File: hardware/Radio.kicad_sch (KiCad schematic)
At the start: 44 parts, among them Q305 BCX56, U801 RF69, U802 AS193-73LF, Y801 32_Mhz

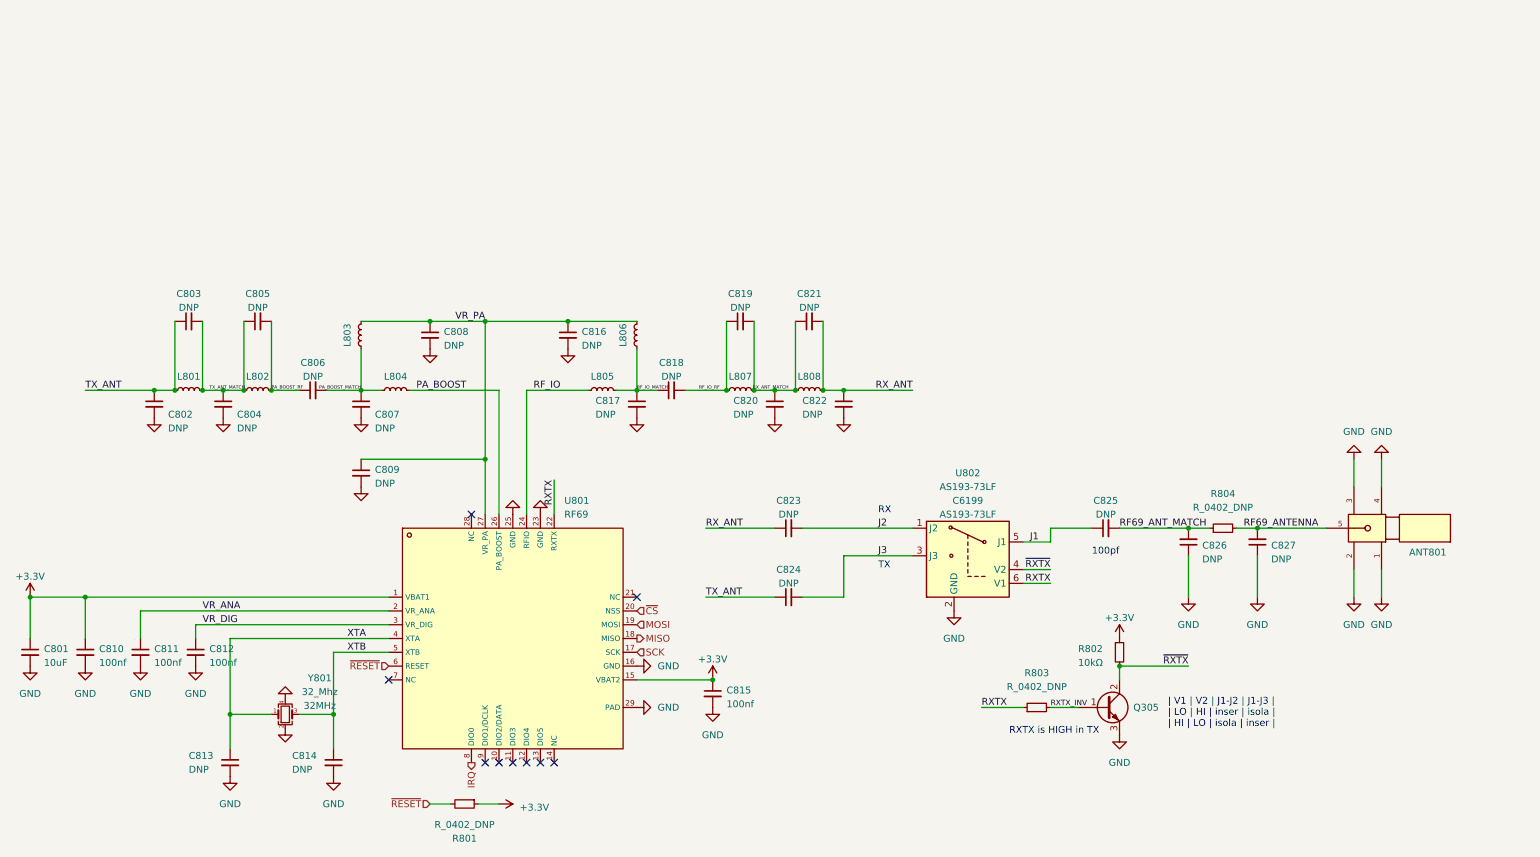
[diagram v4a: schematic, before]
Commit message: RF layout updates
Signed-off-by: Connor Rigby <connorr@hey.com>
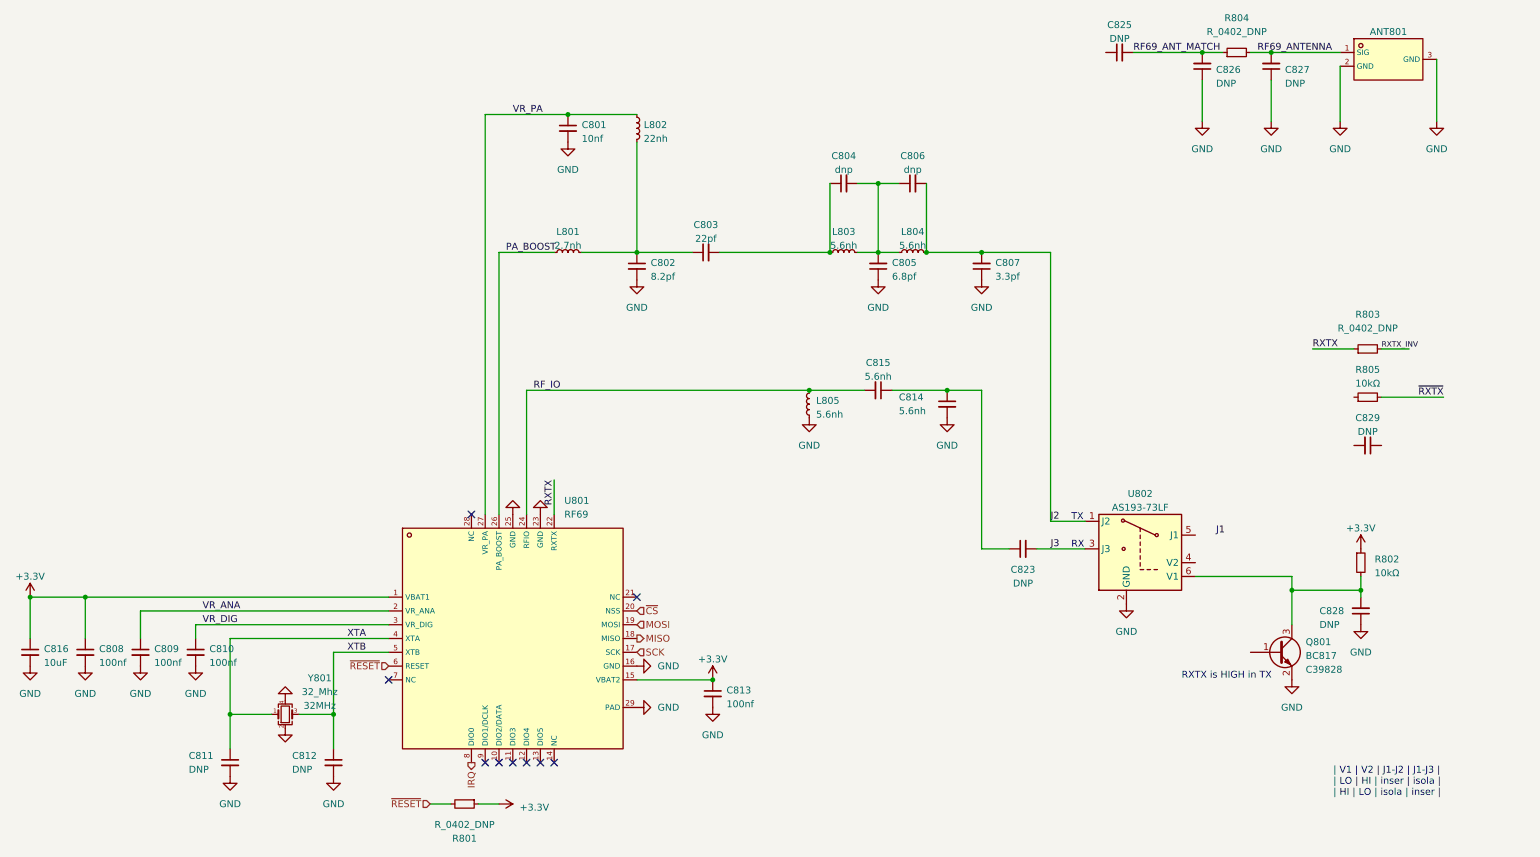
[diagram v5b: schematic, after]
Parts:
- removed ANT801: BWSMA-KE-P001, LCSC_Antenna:SMA-SMD_BWSMA-KE-P001, symbol LCSC_Antenna:BWSMA-KE-P001
- removed C801: C_0805_10u_X5R, Capacitor_SMD:C_0805_2012Metric, symbol LCSC_Capacitor:C_0805_10u_X5R
- removed C808, C809, C816, C817, C818, C819, C820, C821, C822, C824: C_0402_DNP, Capacitor_SMD:C_0402_1005Metric, symbol LCSC_Capacitor:C_0402_DNP
- removed L801, L802, L803, L804, L805, L806, L807, L808: L_0402_DNP, Inductor_SMD:L_0402_1005Metric, symbol LCSC_Inductor:L_0402_DNP
- removed Q305: BCX56, Package_TO_SOT_SMD:SOT-89-3, symbol LCSC_Transistor:BCX56
- added ANT801: BWIPX-1-001E, LCSC_Antenna:IPEX-SMD_BWIPX-1-001E, symbol LCSC_Antenna:BWIPX-1-001E
- added C801, C814, C815, C828, C829: C_0402_DNP, Capacitor_SMD:C_0402_1005Metric, symbol LCSC_Capacitor:C_0402_DNP
- added C816: C_0805_10u_X5R, Capacitor_SMD:C_0805_2012Metric, symbol LCSC_Capacitor:C_0805_10u_X5R
- added L801: 2.7nh, Inductor_SMD:L_0402_1005Metric, symbol Device:L_Small
- added L802: 22nh, Inductor_SMD:L_0402_1005Metric, symbol Device:L_Small
- added L803, L804, L805: 5.6nh, Inductor_SMD:L_0402_1005Metric, symbol Device:L_Small
- added Q801: BC817, Package_TO_SOT_SMD:SOT-23, symbol LCSC_Transistor1:BC817
- added R805: R_0402_10k, Resistor_SMD:R_0402_1005Metric, symbol LCSC_Resistor:R_0402_10k
- C802: Capacitance DNP -> 8.2pf
- C803: Capacitance DNP -> 22pf
- C804, C806: Capacitance DNP -> dnp
- C805: Capacitance DNP -> 6.8pf
- C807: Capacitance DNP -> 3.3pf
- renumbered C810 to C808, C811 to C809, C812 to C810, C813 to C811, C814 to C812, C815 to C813
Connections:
- net +3.3V: now also C816.1
- net GND: now also C805.1, C807.1, ANT801.2 (GND), ANT801.3 (GND), C801.2, C814.2, C816.2, C828.1, L805.1, Q801.2 (E); no longer C804.2, C807.2
- net J1: no longer C825.1, U802.5 (J1)
- net J2: now also C806.2, C807.2, L804.2; no longer C823.2
- net J3: now also C823.2
- net PA_BOOST: now also L801.1
- net RF69_ANTENNA: now also ANT801.1 (SIG)
- net RF_IO: now also C815.2, L805.2
- net RXTX: no longer U802.6 (V1)
- net VR_PA: now also C801.1, L802.1
- net ~{RXTX}: now also R805.2; no longer R802.2, U802.4 (V2)
- removed net PA_BOOST_MATCH: C806.2, C807.1
- net PA_BOOST_RF: no longer names the net of C805.2, C806.1
- net PA_BOOST_RF: now also C804.2, L803.2, L804.1
- net RX_ANT: no longer names the net of C823.1
- net RX_ANT: now also C814.1, C815.1
- net TX_ANT: no longer names the net of C802.1, C803.1
- net TX_ANT: now also L801.2, L802.2
- net TX_ANT_MATCH: no longer names the net of C803.2, C804.1
- net TX_ANT_MATCH: now also L803.1; no longer C805.1
- new net: C828.2, Q801.3 (C), R802.2, U802.6 (V1)
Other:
- note removed: "100pf"
- moved on the sheet: C823, C825, C826, C827, R802, R803, R804, U802

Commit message: Almost ready for fab
Signed-off-by: Connor Rigby <connorr@hey.com>
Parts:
- removed C801, C802, C803, C805, C807, C811, C812, C814, C815, C823, C825, C828, C829: C_0402_DNP, Capacitor_SMD:C_0402_1005Metric, symbol LCSC_Capacitor:C_0402_DNP
- removed L801: 2.7nh, Inductor_SMD:L_0402_1005Metric, symbol Device:L_Small
- removed L802: 22nh, Inductor_SMD:L_0402_1005Metric, symbol Device:L_Small
- removed L803, L804, L805: 5.6nh, Inductor_SMD:L_0402_1005Metric, symbol Device:L_Small
- removed R801, R803, R804: R_0402_DNP, Resistor_SMD:R_0402_1005Metric, symbol LCSC_Resistor:R_0402_DNP
- removed R802: R_0402_10k, Resistor_SMD:R_0402_1005Metric, symbol LCSC_Resistor:R_0402_10k
- added C801: C_0402_10n_C0G, Capacitor_SMD:C_0402_1005Metric, symbol LCSC_Capacitor:C_0402_10n_C0G
- added C802: C_0402_8p2_C0G, Capacitor_SMD:C_0402_1005Metric, symbol LCSC_Capacitor:C_0402_8p2_C0G
- added C803: C_0402_22p_C0G, Capacitor_SMD:C_0402_1005Metric, symbol LCSC_Capacitor:C_0402_22p_C0G
- added C805: C_0402_6p8_C0G, Capacitor_SMD:C_0402_1005Metric, symbol LCSC_Capacitor:C_0402_6p8_C0G
- added C807: C_0402_3p3_C0G, Capacitor_SMD:C_0402_1005Metric, symbol LCSC_Capacitor:C_0402_3p3_C0G
- added C811, C812: C_0402_33p_C0G, Capacitor_SMD:C_0402_1005Metric, symbol LCSC_Capacitor:C_0402_33p_C0G
- added C814: C_0402_5p6_C0G, Capacitor_SMD:C_0402_1005Metric, symbol LCSC_Capacitor:C_0402_5p6_C0G
- added C815, L803, L804: L_0402_5n6, Inductor_SMD:L_0402_1005Metric, symbol LCSC_Inductor:L_0402_5n6
- added C823, C825: C_0402_100p_C0G, Capacitor_SMD:C_0402_1005Metric, symbol LCSC_Capacitor:C_0402_100p_C0G
- added C828, C829: C_0402_1nf_X7R, Capacitor_SMD:C_0402_1005Metric, symbol LCSC_Capacitor:C_0402_1nf_X7R
- added L801: L_0402_2n7, Inductor_SMD:L_0402_1005Metric, symbol LCSC_Inductor:L_0402_2n7
- added L802: L_0402_22n, Inductor_SMD:L_0402_1005Metric, symbol LCSC_Inductor:L_0402_22n
- added L805: L_0402_120n, Inductor_SMD:L_0402_1005Metric, symbol LCSC_Inductor:L_0402_120n
- added R801, R802, R803: R_0402_100k, Resistor_SMD:R_0402_1005Metric, symbol LCSC_Resistor:R_0402_100k
- added R804: R_0402_0, Resistor_SMD:R_0402_1005Metric, symbol LCSC_Resistor:R_0402_0
- C804, C806: Capacitance dnp -> DNP; now not fitted
- C826, C827: now not fitted
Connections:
- net ~{RXTX} is gone; now on net RXTX_NOR: R805.2
- net +3.3V: now also R801.1, R802.1
- net GND: now also C801.2, C802.2, C805.1, C807.1, C811.2, C812.2, C814.2, C828.1, C829.1, L805.1
- net J1: now also U802.5 (J1), C825.1
- net J2: now also C807.2, L804.2
- net J3: now also C823.2
- net PA_BOOST: now also L801.1
- net RF69_ANTENNA: now also R804.2
- net RF69_ANT_MATCH: now also C825.2, R804.1
- net RF_IO: now also C815.2, L805.2
- net RXTX: now also R805.1, R803.1
- net VR_PA: now also C801.1, L802.1
- net XTA: now also C811.1
- net XTB: now also C812.1
- net ~{RESET}: now also R801.2
- net V2: now reaches U802.4 (V2)
- net V2: now also C829.2, R803.2
- net V1: now reaches Q801.3 (C), U802.6 (V1)
- net V1: now also C828.2, R802.2
- net RXTX_NOR: now reaches Q801.1 (B)
- net PA_BOOST_PA_FILTER: now reaches C804.2, C806.1
- net PA_BOOST_PA_FILTER: now also C805.2, L803.2, L804.1
- net PA_BOOST_PA_MATCH: now reaches C804.1
- net PA_BOOST_PA_MATCH: now also C803.2, L803.1
- new net PA_BOOST_PA: C802.1, C803.1, L801.2, L802.2
- new net RFIO_MATCH: C814.1, C815.1, C823.1
- no-connect marks 9 -> 5
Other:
- moved on the sheet: ANT801, Q801, R805

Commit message: Pre-production updates
Signed-off-by: Connor Rigby <connorr@hey.com>
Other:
- company: (none) -> https://cone.codes
- title: (none) -> coneRGB2
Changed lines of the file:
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@@
 (kicad_sch (version 20230121) (generator eeschema)
   (paper "A4")
+  (title_block
+    (title "coneRGB2")
+    (date "2023-03-20")
+    (rev "1")
+    (company "https://cone.codes")
+    (comment 1 "https://github.com/connorrigby/underglow2")
+    (comment 2 "Designed by Connor Rigby")
+    (comment 3 "Handles real time syncronization of installations")
+    (comment 4 "RF69 / SM1231 915mhz Radio")
+  )
   (junction (at 184.15 63.5) (diameter 0) (color 0 0 0 0)
   )
@@
     (stroke (width 0) (type default))
   )
-  (wire (pts (xy 190.5 139.7) (xy 213.36 139.7))
+  (wire (pts (xy 177.8 139.7) (xy 213.36 139.7))
     (stroke (width 0) (type default))
   )
@@
     (stroke (width 0) (type default))
   )
+  (wire (pts (xy 177.8 101.6) (xy 177.8 139.7))
+    (stroke (width 0) (type default))
+  )
   (wire (pts (xy 203.2 113.03) (xy 203.2 63.5))
     (stroke (width 0) (type default))
@@
     (stroke (width 0) (type default))
   )
-  (wire (pts (xy 111.76 105.41) (xy 111.76 111.76))
+  (wire (pts (xy 111.76 101.6) (xy 111.76 111.76))
     (stroke (width 0) (type default))
   )
@@
     (stroke (width 0) (type default))
   )
+  (wire (pts (xy 111.76 101.6) (xy 177.8 101.6))
+    (stroke (width 0) (type default))
+  )
   (wire (pts (xy 78.74 139.7) (xy 81.28 139.7))
     (stroke (width 0) (type default))
@@
   (wire (pts (xy 254 152.4) (xy 266.7 152.4))
     (stroke (width 0) (type default))
+  )
+  (text_box "Testing required: automotive use may require a TXCO instead of a simple crystal oscilator"
+    (at 25.4 152.4 0) (size 21.59 11.43)
+    (stroke (width 0) (type default))
+    (fill (type none))
+    (effects (font (size 1.27 1.27)) (justify left top))
+  )
+  (text_box "RF Switch to allow TX and RX to share the same antenna.\nSwitched by the RXTX GPO from the IC. \nTransistor + pullups invert that signal to keep the switch\nin a valid state. See truth table below.\n1nF caps taken from the RF69 Module layout. Assuming for a debounce\nor RC filter to smooth transisitions from TX to RX and back. Not in reference design"
+    (at 246.38 85.09 0) (size 36.83 30.48)
+    (stroke (width 0) (type default))
+    (fill (type none))
+    (effects (font (size 1.27 1.27)) (justify left top))
+  )
+  (text_box "Reference design: -17dBm configuration\ncomponent values are from the reference design as I do not have\nexpensive spectrum analyzing equipment. \n\nDNP footprints are reserved, but are not populated."
+    (at 152.4 25.4 0) (size 52.07 13.97)
+    (stroke (width 0) (type default))
+    (fill (type none))
+    (effects (font (size 1.27 1.27)) (justify left top))
+  )
+  (text_box "I-PEX 1 Connector and matching network.\nLeft unpopulated with a jumper resistor in place of\nthe inductor."
+    (at 226.06 49.53 0) (size 52.07 7.62)
+    (stroke (width 0) (type default))
+    (fill (type none))
+    (effects (font (size 1.27 1.27)) (justify left top))
   )
   (text "RXTX is HIGH in TX" (at 190.5 142.24 0)
@@
     )
   )
-  (label "RXTX" (at 111.76 105.41 270) (fields_autoplaced)
-    (effects (font (size 1.27 1.27)) (justify right bottom))
-  )
   (label "XTB" (at 73.66 137.16 0) (fields_autoplaced)

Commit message: Submitted for production
Signed-off-by: Connor Rigby <connorr@hey.com>
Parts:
- added AE801: SMA_Antenna_915mhz, Enclosure:SMA_Antenna_Vertical, symbol Device:Antenna
- added AE802: SMA_IPX_Cable, Enclosure:SMA_Connector, symbol Device:Antenna
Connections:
- no-connect marks 5 -> 7
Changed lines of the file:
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@@
   (junction (at 234.95 63.5) (diameter 0) (color 0 0 0 0)
   )
+  (no_connect (at 76.2 43.18))
   (no_connect (at 101.6 157.48))
+  (no_connect (at 38.1 43.18))
   (no_connect (at 104.14 157.48))
   (no_connect (at 99.06 157.48))
@@
     (stroke (width 0) (type default))
   )
+  (rectangle (start 25.4 25.4) (end 88.9 50.8)
+    (stroke (width 0) (type default))
+    (fill (type none))
+  )
   (text_box "Testing required: automotive use may require a TXCO instead of a simple crystal oscilator"
     (at 25.4 152.4 0) (size 21.59 11.43)
@@
     )
   )
+  (symbol (lib_id "Device:Antenna") (at 38.1 38.1 0) (unit 1)
+    (in_bom yes) (on_board no) (dnp no)
+    (property "Reference" "AE801" (at 30.48 30.48 0)
+      (effects (font (size 1.27 1.27)) (justify left))
+    )
+    (property "Value" "SMA_Antenna_915mhz" (at 30.48 33.02 0)
+      (effects (font (size 1.27 1.27)) (justify left))
+    )
+    (property "Footprint" "Enclosure:SMA_Antenna_Vertical" (at 38.1 38.1 0)
+      (effects (font (size 1.27 1.27)) hide)
+    )
+    (property "Datasheet" "https://datasheet.lcsc.com/lcsc/2207191000_ZIISOR-TX915-JK-11_C468327.pdf" (at 38.1 38.1 0)
+      (effects (font (size 1.27 1.27)) hide)
+    )
+    (property "MPN" "TX915-JK-11" (at 38.1 38.1 0)
+      (effects (font (size 1.27 1.27)) hide)
+    )
+    (property "LCSC" "C468327" (at 38.1 38.1 0)
+      (effects (font (size 1.27 1.27)) hide)
+    )
+    (pin "1")
+    (instances
+      (project "underglow2"
+        (path "/dcbdf88a-d6ac-4b1d-9514-0b0ce113d90b/bab1dc88-b79a-454f-b699-1d1b3e7eefdd"
+          (reference "AE801") (unit 1)
+        )
+      )
+    )
+  )
   (symbol (lib_id "power:GND") (at 15.24 139.7 0) (unit 1)
     (in_bom yes) (on_board yes) (dnp no) (fields_autoplaced)
@@
         )
       )
+    )
+  )
+  (symbol (lib_id "Device:Antenna") (at 76.2 38.1 0) (unit 1)
+    (in_bom yes) (on_board no) (dnp no)
+    (property "Reference" "AE802" (at 69.85 30.48 0)
+      (effects (font (size 1.27 1.27)) (justify left))
+    )
+    (property "Value" "SMA_IPX_Cable" (at 69.85 33.02 0)
+      (effects (font (size 1.27 1.27)) (justify left))
+    )
+    (property "Footprint" "Enclosure:SMA_Connector" (at 76.2 38.1 0)
+      (effects (font (size 1.27 1.27)) hide)
+    )
+    (property "Datasheet" "https://datasheet.lcsc.com/lcsc/2009180306_BAT-WIRELESS-BWIPX1-SMA-1-13L100_C784403.pdf" (at 76.2 38.1 0)
+      (effects (font (size 1.27 1.27)) hide)
+    )
+    (property "LCSC" "C784403" (at 76.2 38.1 0)
+      (effects (font (size 1.27 1.27)) hide)
+    )
+    (property "MPN" "BWIPX1-SMA-1.13L100" (at 76.2 38.1 0)
+      (effects (font (size 1.27 1.27)) hide)
+    )
+    (pin "1")
+    (instances
+      (project "underglow2"
+        (path "/dcbdf88a-d6ac-4b1d-9514-0b0ce113d90b/bab1dc88-b79a-454f-b699-1d1b3e7eefdd"
+          (reference "AE802") (unit 1)
+        )
+      )
